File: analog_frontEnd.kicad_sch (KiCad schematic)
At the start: 18 parts, among them U601 TLV9061SIDBVR, U602 TLV9061SIDBVR

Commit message: Updated Schematic v1.0
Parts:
- TP603: footprint 0_testpoints:TestPoint_NoSlik_D0.5mm_Bottom -> 0_testpoints:TestPoint_NoSlik_D0.5mm_Top
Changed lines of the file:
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@@
 			)
 		)
-		(property "Footprint" "0_testpoints:TestPoint_NoSlik_D0.5mm_Bottom"
+		(property "Footprint" "0_testpoints:TestPoint_NoSlik_D0.5mm_Top"
 			(at 342.9 114.3 0)
 			(hide yes)
@@
 			(at 342.9 109.22 0)
 			(hide yes)
+			(show_name no)
+			(do_not_autoplace no)
+			(effects
+				(font
+					(size 1.27 1.27)
+				)
+			)
+		)
+		(property "Manufacturer" ""
+			(at 342.9 109.22 0)
+			(hide yes)
+			(show_name no)
+			(do_not_autoplace no)
+			(effects
+				(font
+					(size 1.27 1.27)
+				)
+			)
+		)
+		(property "Manufacturer Part Number" ""
+			(at 342.9 109.22 0)
+			(hide yes)
+			(show_name no)
+			(do_not_autoplace no)
+			(effects
+				(font
+					(size 1.27 1.27)
+				)
+			)
+		)
+		(property "Supplier Part Number" ""
+			(at 342.9 109.22 0)
+			(hide yes)
+			(show_name no)
+			(do_not_autoplace no)
+			(effects
+				(font
+					(size 1.27 1.27)
+				)
+			)
+		)
+		(property "Supplier" ""
+			(at 342.9 109.22 0)
+			(hide yes)
+			(show_name no)
+			(do_not_autoplace no)
+			(effects
+				(font
+					(size 1.27 1.27)
+				)
+			)
+		)
+		(property "Manufacturer 2nd" ""
+			(at 342.9 109.22 0)
+			(hide yes)
+			(show_name no)
+			(do_not_autoplace no)
+			(effects
+				(font
+					(size 1.27 1.27)
+				)
+			)
+		)
+		(property "Manufacturer Part Number 2nd" ""
+			(at 342.9 109.22 0)
+			(hide yes)
+			(show_name no)
+			(do_not_autoplace no)
+			(effects
+				(font
+					(size 1.27 1.27)
+				)
+			)
+		)
+		(property "Supplier Part Number 2nd" ""
+			(at 342.9 109.22 0)
+			(hide yes)
+			(show_name no)
+			(do_not_autoplace no)
+			(effects
+				(font
+					(size 1.27 1.27)
+				)
+			)
+		)
+		(property "Supplier 2nd" ""
+			(at 342.9 109.22 0)
+			(hide yes)

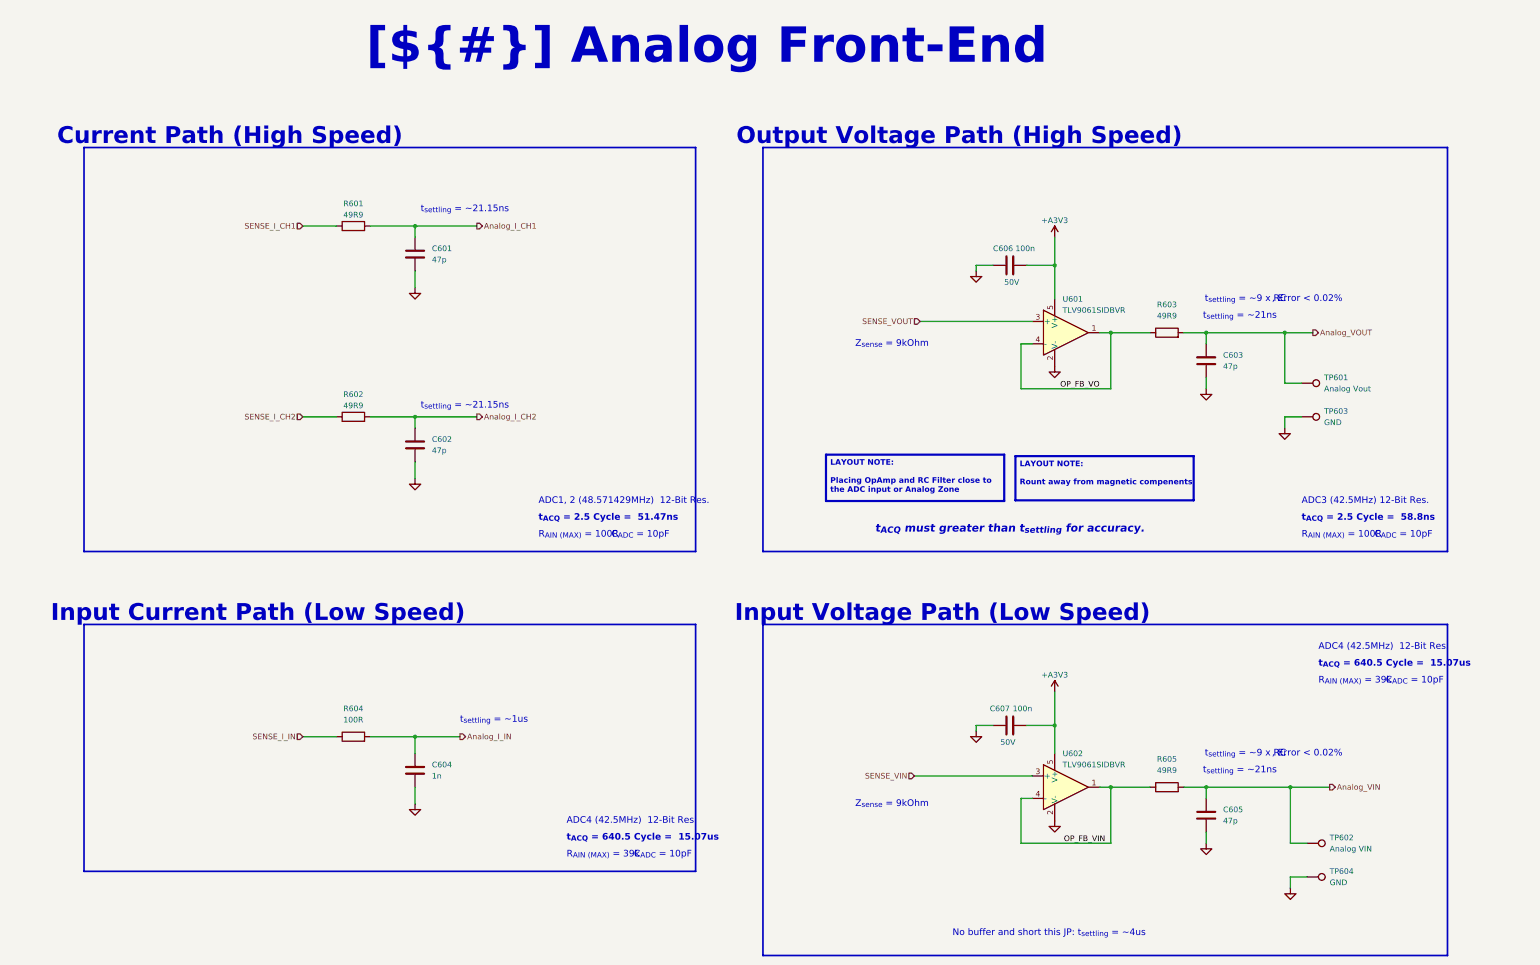
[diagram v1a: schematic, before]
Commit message: Rev1.1
- Removed the Mosfet that Enable the ICs Gate Driver (p.1)
- Changed ADC input Capacitor 47pF to 1nF. (p.6
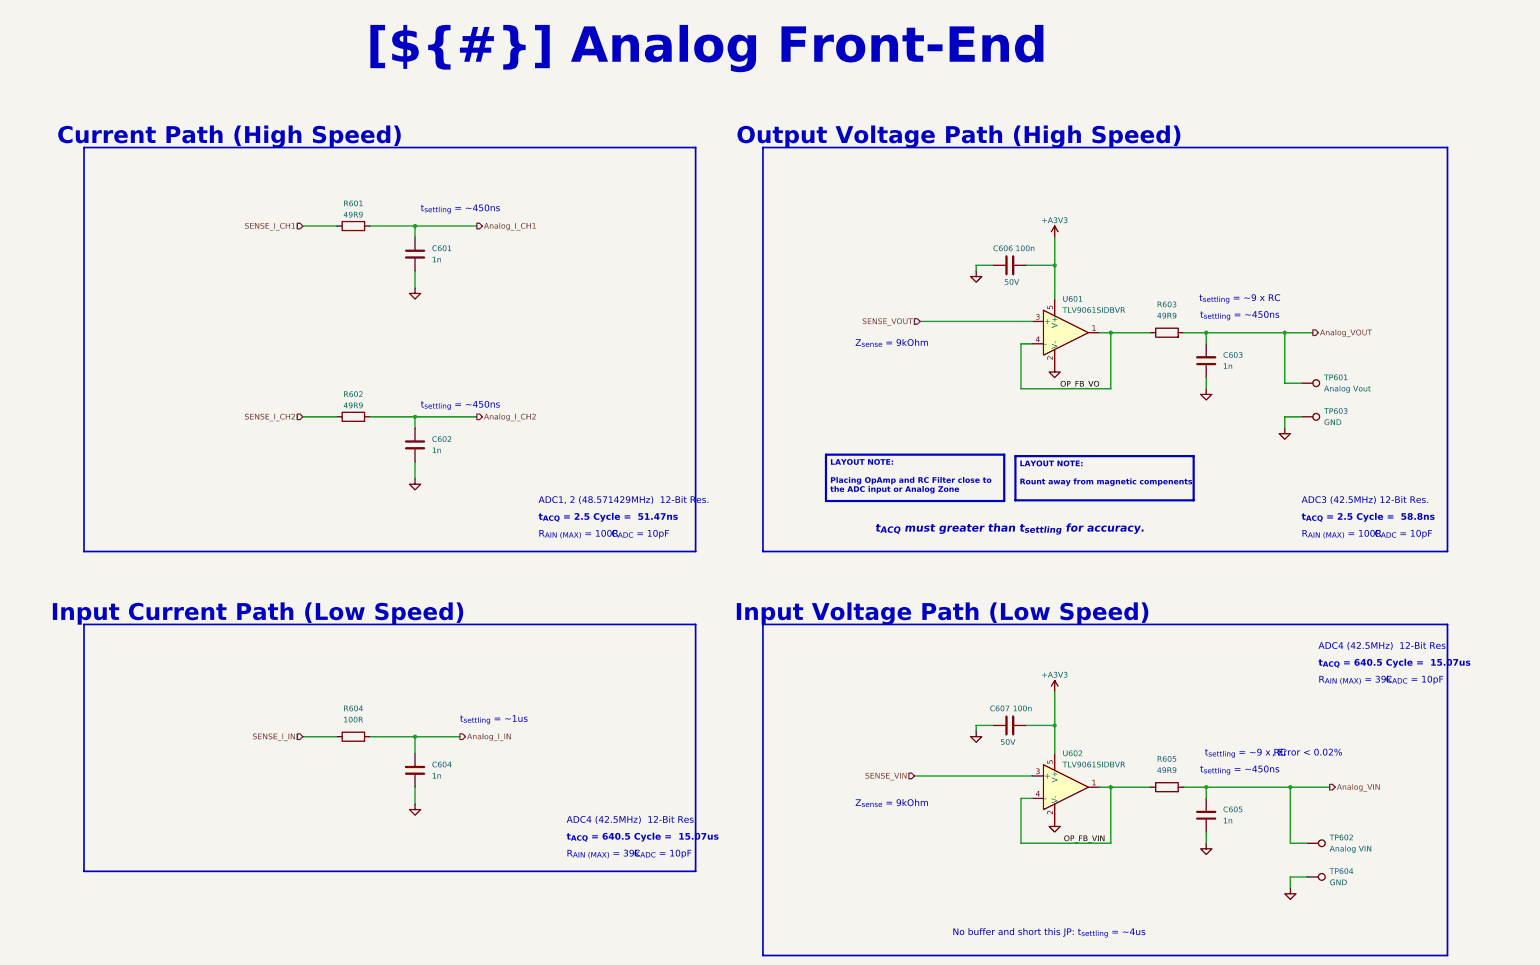
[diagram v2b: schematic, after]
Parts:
- C601, C602, C603, C605: value 47p -> 1n; Manufacturer 2nd KYOCERA AVX -> Murata; Manufacturer Part Number GRM1555C1H470GA01D -> GRM1555C1H102JA01D; Manufacturer Part Number 2nd 04025A470JAT2A -> GRM1555C1H102JA01D; Supplier Part Number 490-8206-1-ND -> 490-3244-1-ND; Supplier Part Number 2nd 0092-0407-5 -> 0160-0208-1
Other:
- note added: "t_{settling} = ~450ns"
- note removed: "t_{settling} = ~21.15ns"
- note removed: "t_{settling} = ~21ns"
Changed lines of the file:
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@@
 	(paper "A3")
 	(title_block
-		(rev "1.0")
+		(rev "1.1")
 		(comment 1 "Analog Front-End")
 	)
@@
 		)
 	)
-	(text ", Error < 0.02%"
-		(exclude_from_sim no)
-		(at 344.17 82.55 0)
-		(effects
-			(font
-				(size 1.5 1.5)
-			)
-		)
-	)
 	(text "R_{AIN (MAX)} = 39k"
 		(exclude_from_sim no)
@@
 		)
 	)
-	(text "t_{settling} = ~21.15ns"
+	(text "t_{settling} = ~450ns"
 		(exclude_from_sim no)
 		(at 143.51 62.23 0)
@@
 		)
 	)
-	(text "t_{settling} = ~21.15ns"
+	(text "t_{settling} = ~450ns"
 		(exclude_from_sim no)
 		(at 143.51 106.68 0)
@@
 		)
 	)
-	(text "t_{settling} = ~21ns"
+	(text "t_{settling} = ~450ns"
 		(exclude_from_sim no)
 		(at 328.93 86.36 0)
@@
 	(text "t_{settling} = ~9 x RC "
 		(exclude_from_sim no)
-		(at 330.2 82.55 0)
+		(at 328.93 82.55 0)
 		(effects
 			(font
@@
 		)
 	)
-	(text "t_{settling} = ~21ns"
+	(text "t_{settling} = ~450ns"
 		(exclude_from_sim no)
 		(at 328.93 189.23 0)
@@
 			)
 		)
-		(property "Value" "47p"
+		(property "Value" "1n"
 			(at 325.12 97.79 0)
 			(show_name no)
@@
 			)
 		)
-		(property "Manufacturer Part Number" "GRM1555C1H470GA01D"
+		(property "Manufacturer Part Number" "GRM1555C1H102JA01D"
 			(at 321.31 96.52 0)
 			(hide yes)
@@
 			)
 		)
-		(property "Supplier Part Number" "490-8206-1-ND"
+		(property "Supplier Part Number" "490-3244-1-ND"
 			(at 321.31 96.52 0)
 			(hide yes)
@@
 			)
 		)
-		(property "Manufacturer 2nd" "KYOCERA AVX"
+		(property "Manufacturer 2nd" "Murata"
 			(at 321.31 96.52 0)
 			(hide yes)
@@
 			)
 		)
-		(property "Manufacturer Part Number 2nd" "04025A470JAT2A"
+		(property "Manufacturer Part Number 2nd" "GRM1555C1H102JA01D"
 			(at 321.31 96.52 0)
 			(hide yes)
@@
 			)
 		)
-		(property "Supplier Part Number 2nd" "0092-0407-5"
+		(property "Supplier Part Number 2nd" "0160-0208-1"
 			(at 321.31 96.52 0)
 			(hide yes)
@@
 			)
 		)
-		(property "Value" "47p"
+		(property "Value" "1n"
 			(at 146.05 116.84 0)
 			(show_name no)
@@
 			)
 		)
-		(property "Manufacturer Part Number" "GRM1555C1H470GA01D"
+		(property "Manufacturer Part Number" "GRM1555C1H102JA01D"
 			(at 142.24 115.57 0)
 			(hide yes)
@@
 			)
 		)
-		(property "Supplier Part Number" "490-8206-1-ND"
+		(property "Supplier Part Number" "490-3244-1-ND"
 			(at 142.24 115.57 0)
 			(hide yes)
@@
 			)
 		)
-		(property "Manufacturer 2nd" "KYOCERA AVX"
+		(property "Manufacturer 2nd" "Murata"
 			(at 142.24 115.57 0)
 			(hide yes)
@@
 			)
 		)
-		(property "Manufacturer Part Number 2nd" "04025A470JAT2A"
+		(property "Manufacturer Part Number 2nd" "GRM1555C1H102JA01D"
 			(at 142.24 115.57 0)
 			(hide yes)
@@
 			)
 		)
-		(property "Supplier Part Number 2nd" "0092-0407-5"
+		(property "Supplier Part Number 2nd" "0160-0208-1"
 			(at 142.24 115.57 0)
 			(hide yes)
@@
 			)
 		)
-		(property "Value" "47p"
+		(property "Value" "1n"
 			(at 146.05 73.66 0)
 			(show_name no)
@@
 			)
 		)
-		(property "Manufacturer Part Number" "GRM1555C1H470GA01D"
+		(property "Manufacturer Part Number" "GRM1555C1H102JA01D"
 			(at 142.24 72.39 0)
 			(hide yes)
@@
 			)
 		)
-		(property "Supplier Part Number" "490-8206-1-ND"
+		(property "Supplier Part Number" "490-3244-1-ND"
 			(at 142.24 72.39 0)
 			(hide yes)
@@
 			)
 		)
-		(property "Manufacturer 2nd" "KYOCERA AVX"
+		(property "Manufacturer 2nd" "Murata"
 			(at 142.24 72.39 0)
 			(hide yes)
@@
 			)
 		)
-		(property "Manufacturer Part Number 2nd" "04025A470JAT2A"
+		(property "Manufacturer Part Number 2nd" "GRM1555C1H102JA01D"
 			(at 142.24 72.39 0)
 			(hide yes)
@@
 			)
 		)
-		(property "Supplier Part Number 2nd" "0092-0407-5"
+		(property "Supplier Part Number 2nd" "0160-0208-1"
 			(at 142.24 72.39 0)
 			(hide yes)
@@
 			)
 		)
-		(property "Value" "47p"
+		(property "Value" "1n"
 			(at 325.12 200.66 0)
 			(show_name no)
@@
 			)
 		)
-		(property "Manufacturer Part Number" "GRM1555C1H470GA01D"
+		(property "Manufacturer Part Number" "GRM1555C1H102JA01D"
 			(at 321.31 199.39 0)
 			(hide yes)
@@
 			)
 		)
-		(property "Supplier Part Number" "490-8206-1-ND"
+		(property "Supplier Part Number" "490-3244-1-ND"
 			(at 321.31 199.39 0)
 			(hide yes)
@@
 			)
 		)
-		(property "Manufacturer 2nd" "KYOCERA AVX"
+		(property "Manufacturer 2nd" "Murata"
 			(at 321.31 199.39 0)
 			(hide yes)
@@
 			)
 		)
-		(property "Manufacturer Part Number 2nd" "04025A470JAT2A"
+		(property "Manufacturer Part Number 2nd" "GRM1555C1H102JA01D"
 			(at 321.31 199.39 0)
 			(hide yes)
@@
 			)
 		)
-		(property "Supplier Part Number 2nd" "0092-0407-5"
+		(property "Supplier Part Number 2nd" "0160-0208-1"
 			(at 321.31 199.39 0)
 			(hide yes)
